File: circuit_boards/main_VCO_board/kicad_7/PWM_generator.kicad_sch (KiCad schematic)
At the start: 24 parts, among them Q601 MMBT3904, U1 TL072, U5 TL072

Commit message: Progress on circuit boards
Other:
- moved on the sheet: C602, C603, D601, D602, D603, Q601, R601, R602, R605, R606, R607, R608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

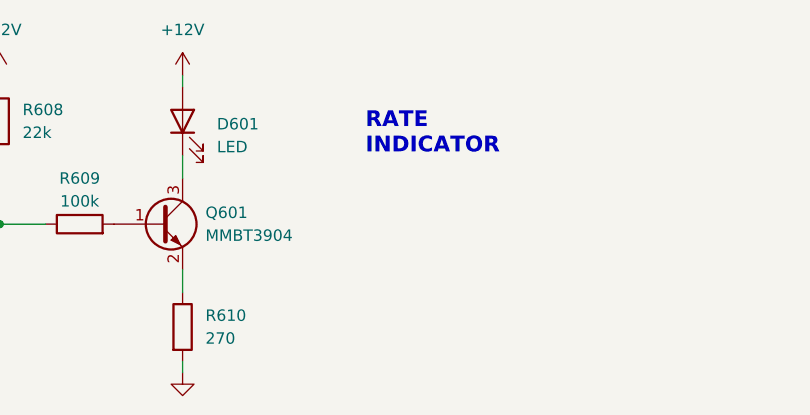
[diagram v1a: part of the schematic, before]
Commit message: Update PCBs, tweak vals, add VCF CV from DAC
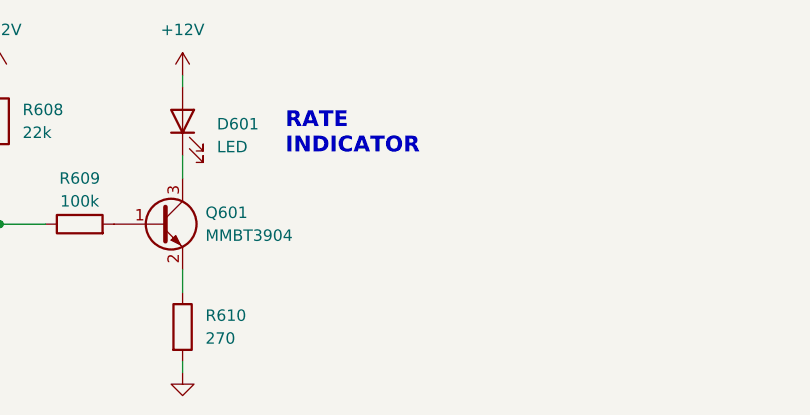
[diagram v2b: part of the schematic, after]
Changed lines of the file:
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@@
     (effects (font (size 1.75 1.75) (thickness 0.35) bold) (justify left bottom))
   )
-  (text "RATE\nINDICATOR" (at 196.85 46.99 0)
+  (text "RATE\nINDICATOR" (at 187.96 46.99 0)
     (effects (font (size 1.75 1.75) (thickness 0.35) bold) (justify left bottom))
   )

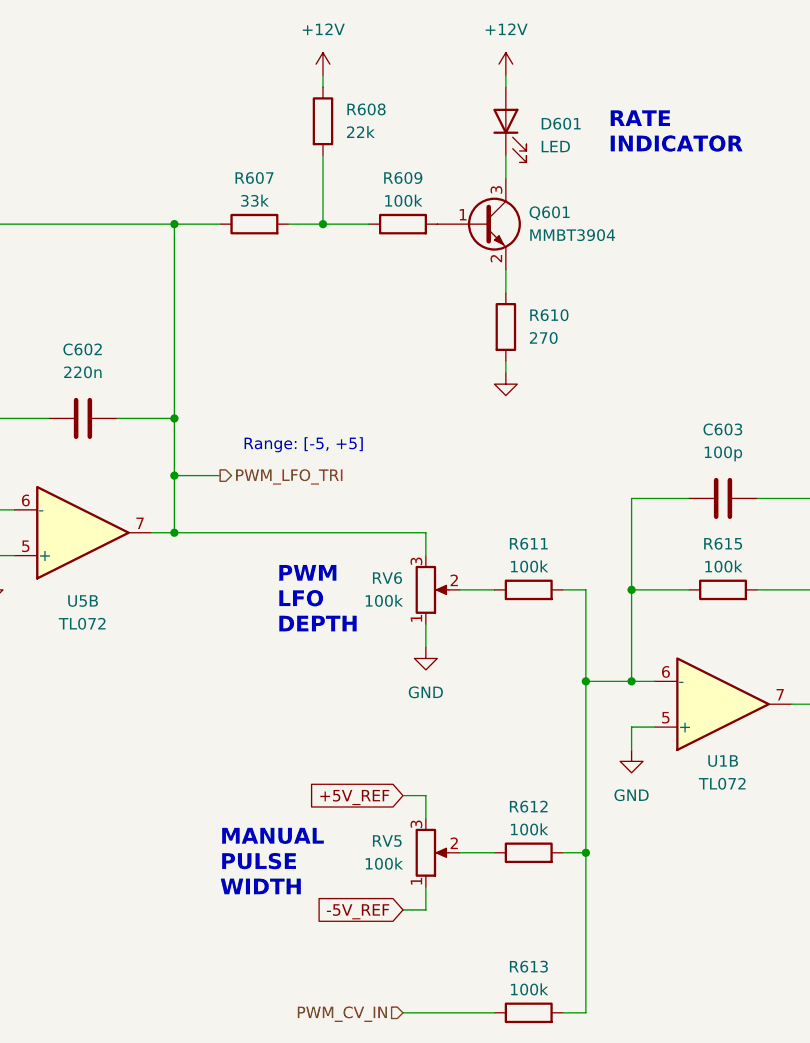
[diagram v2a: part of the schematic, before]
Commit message: Resistor tweaks while evaluating 1st build
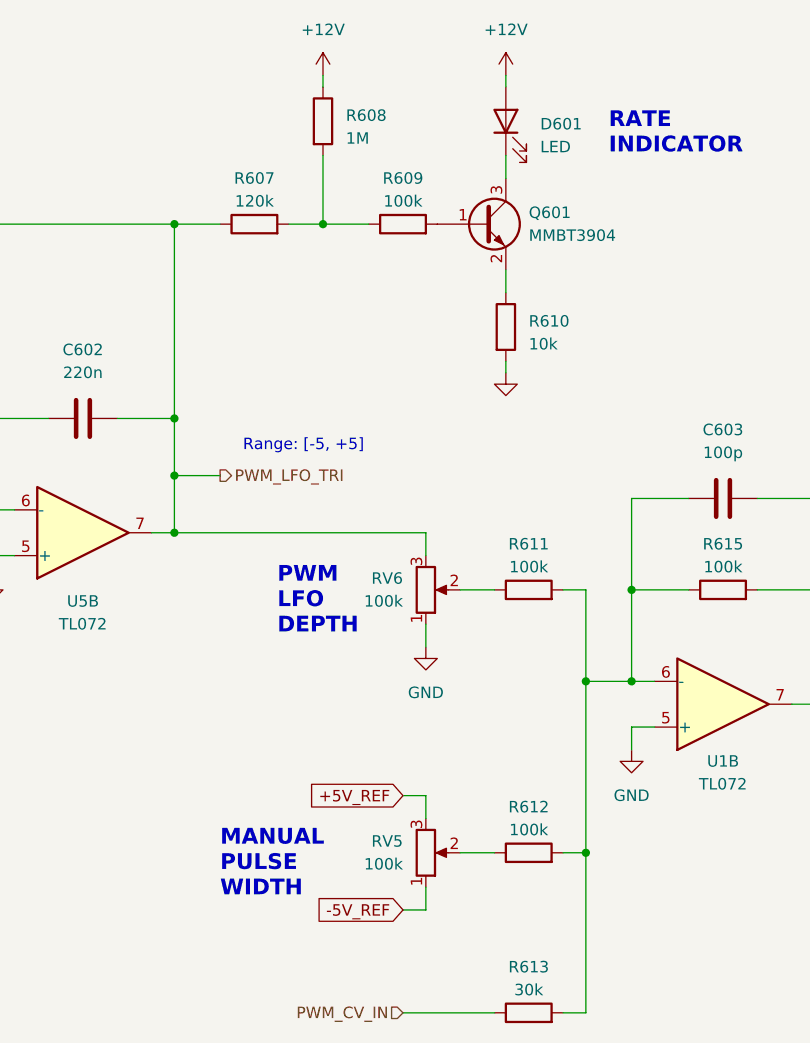
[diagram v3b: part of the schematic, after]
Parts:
- R607: value 33k -> 120k
- R608: value 22k -> 1M
- R610: value 270 -> 10k
- R613: value 100k -> 30k
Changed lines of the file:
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@@
       (effects (font (size 1.27 1.27)))
     )
-    (property "Value" "33k" (at 148.59 52.07 90)
+    (property "Value" "120k" (at 148.59 52.07 90)
       (effects (font (size 1.27 1.27)))
     )
@@
   (symbol (lib_id "Device:R") (at 156.21 43.18 0) (unit 1)
     (in_bom yes) (on_board yes) (dnp no) (fields_autoplaced)
-    (property "Reference" "R608" (at 158.75 41.91 0)
-      (effects (font (size 1.27 1.27)) (justify left))
-    )
-    (property "Value" "22k" (at 158.75 44.45 0)
+    (property "Reference" "R608" (at 158.75 42.545 0)
+      (effects (font (size 1.27 1.27)) (justify left))
+    )
+    (property "Value" "1M" (at 158.75 45.085 0)
       (effects (font (size 1.27 1.27)) (justify left))
     )
@@
   (symbol (lib_id "Device:R") (at 176.53 66.04 0) (unit 1)
     (in_bom yes) (on_board yes) (dnp no) (fields_autoplaced)
-    (property "Reference" "R610" (at 179.07 64.77 0)
-      (effects (font (size 1.27 1.27)) (justify left))
-    )
-    (property "Value" "270" (at 179.07 67.31 0)
+    (property "Reference" "R610" (at 179.07 65.405 0)
+      (effects (font (size 1.27 1.27)) (justify left))
+    )
+    (property "Value" "10k" (at 179.07 67.945 0)
       (effects (font (size 1.27 1.27)) (justify left))
     )
@@
       (effects (font (size 1.27 1.27)))
     )
-    (property "Value" "100k" (at 179.07 139.7 90)
-      (effects (font (size 1.27 1.27)))
-    )
+    (property "Value" "30k" (at 179.07 139.7 90)
+      (effects (font (size 1.27 1.27)))
+    )

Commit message: Add potentiometer 3d model to VCO and MOD boards
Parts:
- RV4, RV5, RV6: footprint Potentiometer_THT:Potentiometer_Alpha_RD901F-40-00D_Single_Vertical -> custom_footprints:Potentiometer_Alpha_RD901F-40-00D_Single_Vertical
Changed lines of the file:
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@@
       (effects (font (size 1.27 1.27)) (justify right))
     )
-    (property "Footprint" "Potentiometer_THT:Potentiometer_Alpha_RD901F-40-00D_Single_Vertical" (at 167.64 95.25 0)
+    (property "Footprint" "custom_footprints:Potentiometer_Alpha_RD901F-40-00D_Single_Vertical" (at 167.64 95.25 0)
       (effects (font (size 1.27 1.27)) hide)
     )
@@
       (effects (font (size 1.27 1.27)) (justify right))
     )
-    (property "Footprint" "Potentiometer_THT:Potentiometer_Alpha_RD901F-40-00D_Single_Vertical" (at 91.44 86.36 0)
+    (property "Footprint" "custom_footprints:Potentiometer_Alpha_RD901F-40-00D_Single_Vertical" (at 91.44 86.36 0)
       (effects (font (size 1.27 1.27)) hide)
     )
@@
       (effects (font (size 1.27 1.27)) (justify right))
     )
-    (property "Footprint" "Potentiometer_THT:Potentiometer_Alpha_RD901F-40-00D_Single_Vertical" (at 167.64 124.46 0)
-      (effects (font (size 1.27 1.27)) hide)
-    )
+    (property "Footprint" "custom_footprints:Potentiometer_Alpha_RD901F-40-00D_Single_Vertical" (at 167.64 124.46 0)
+      (effects (font (size 1.27 1.27)) hide)
+    )
